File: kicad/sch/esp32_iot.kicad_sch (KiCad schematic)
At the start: 11 parts, among them J60 CAMPO / ETHERNET, SW60 ESP_EN, SW61 ESP_BOOT, U60 ESP32-S3-WROOM-1-N8

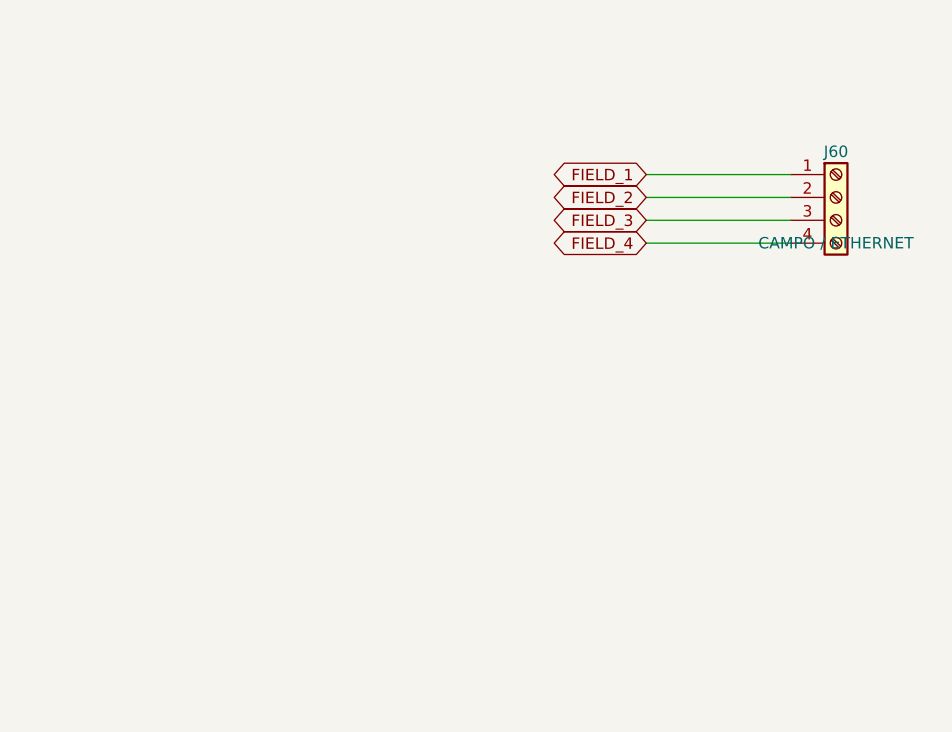
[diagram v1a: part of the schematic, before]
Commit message: Anade protecciones electricas y stackup con color
PROTECCIONES (de 15 a 56 componentes de proteccion, 272 en total)

  12x TVS gate-source, una por SiC. Sin ella un pico de dv/dt acoplado
      por Cgd puede perforar el oxido de puerta: es el modo de fallo mas
      comun en SiC. Va en el pie del transistor.
  12x snubber RC del nodo de conmutacion (220 pF + 4.7 ohm). El valor sale
      del barrido en LTspice: baja el dv/dt de 147 a 90 V/ns, por debajo
      del CMTI de 100 V/ns del UCC21520, y la sobretension de 823 a 767 V.
   2x TVS en serie sobre el bus DC (5KP440A): recorte en nanosegundos muy
      por delante del chopper, que es un lazo de control.
  12x Schottky de recorte en las entradas de ADC. La R serie del filtro
      anti-alias limita la corriente; sin los diodos, un transitorio de la
      etapa de potencia entra directo al pin del STM32.
   4x TVS de ESD en el conector de campo del ESP32.
   1x polyfuse rearmable + diodo antiinversion + TVS en la entrada de 24 V.

BUGS DESTAPADOS AL CABLEAR LAS PROTECCIONES

  a) Los 4 TVS del conector de campo compartian columna: sus bajadas a
     IOGND se solapaban y cortocircuitaban las cuatro lineas. Cada uno a
     su propia x.
  b) Los diodos de recorte del ADC morian en MITAD del cable de senal, asi
     que KiCad no los conectaba (solo une extremo con extremo, el mismo
     fallo que ya aparecio en los rieles del bus). El cable se parte ahora
     en el punto de recorte.

ASPECTO

  El .kicad_pcb no tenia seccion (stackup), por eso el render salia verde
  por defecto. Se inyecta desde tools/stackup_tpl.txt: mascara negra,
  serigrafia blanca, acabado ENIG (obligado con el LQFP-100 de paso
  0.5 mm) y los espesores reales de cobre (70 um exteriores, 35 um
  interiores) con prepreg fino de 0.2 mm entre F.Cu e In1.Cu para que el
  bus laminado tenga poca inductancia. Los colores son parametros al
  principio de tools/gen_pcb.py.

Co-Authored-By: Claude Opus 5 <noreply@anthropic.com>
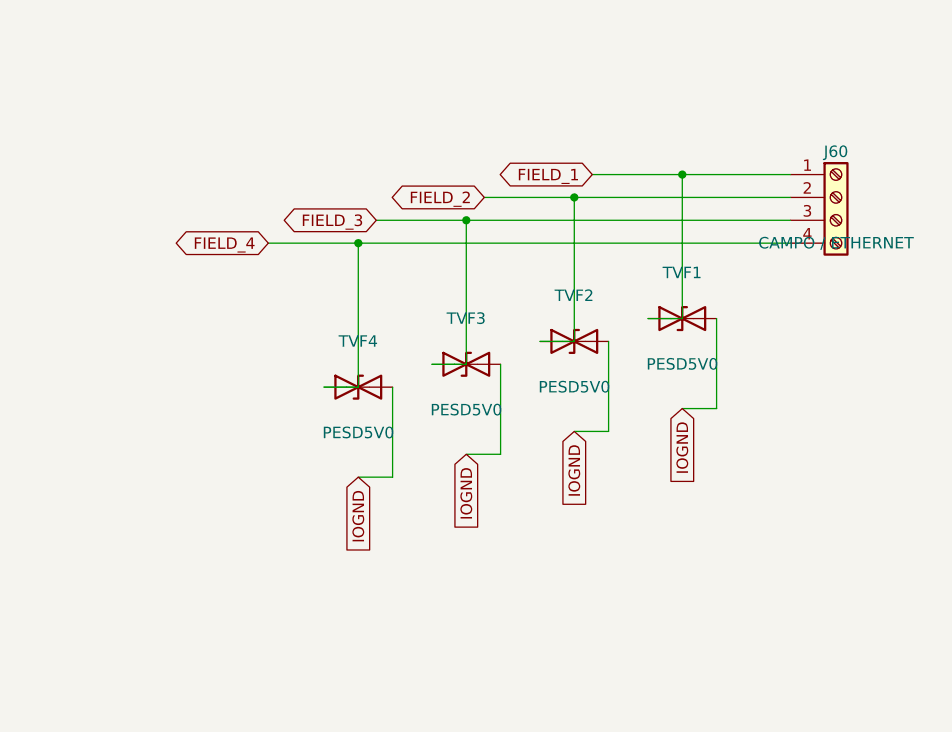
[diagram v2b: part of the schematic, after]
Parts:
- added TVF1, TVF2, TVF3, TVF4: PESD5V0, Diode_SMD:D_SOD-123, symbol Device:D_TVS
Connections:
- net FIELD_1: now also TVF1.1 (A1)
- net FIELD_2: now also TVF2.1 (A1)
- net FIELD_3: now also TVF3.1 (A1)
- net FIELD_4: now also TVF4.1 (A1)
- net IOGND: now also TVF1.2 (A2), TVF2.2 (A2), TVF3.2 (A2), TVF4.2 (A2)
